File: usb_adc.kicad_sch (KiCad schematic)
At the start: 17 parts, among them IC1 PCM2903CDBR, U3 74LVC1G08, X1 ECS-120-8-36-CKM-TR3

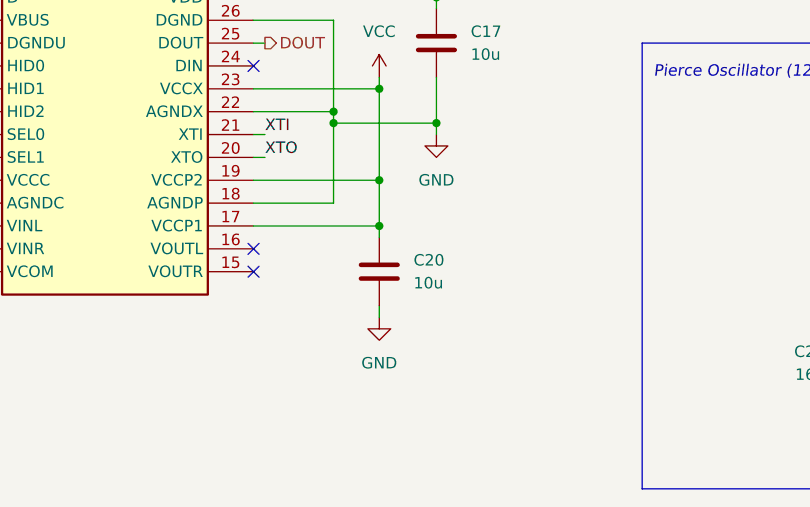
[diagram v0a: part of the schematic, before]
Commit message: Removed S/PIDF and still doing layout
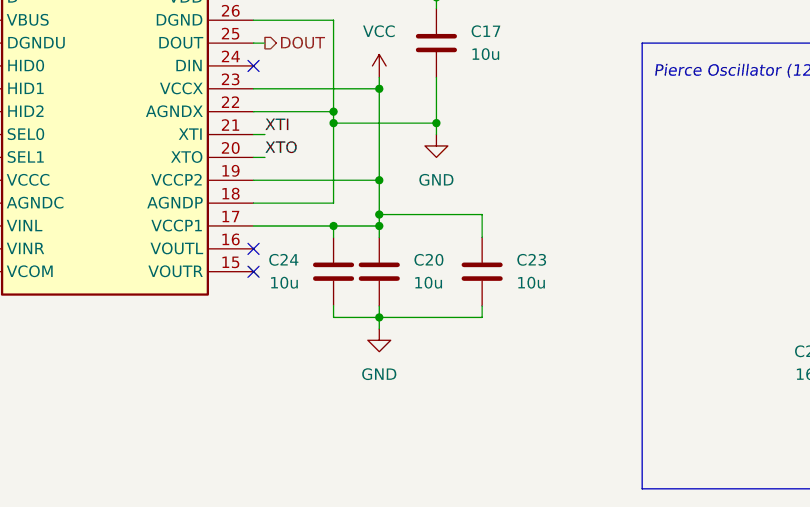
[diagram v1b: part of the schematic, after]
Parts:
- added C23, C24: 10u, Capacitor_SMD:C_0805_2012Metric_Pad1.18x1.45mm_HandSolder, symbol Device:C
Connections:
- net GND: now also C23.2, C24.2
- net VCC: now also C23.1, C24.1

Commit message: More layout, replaced chip crystal with a 2-pin oscillator
All is well with the world
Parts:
- removed X1: ECS-120-8-36-CKM-TR3, binauralmic:ECS120836CKMTR3, symbol Device:Crystal_GND24
- added Y1: ABLS-12.000MHZ-20-D-3-H-T, binauralmic:ABLS, symbol Device:Crystal
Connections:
- net XTI: now also Y1.1
- net XTO: now also Y1.2
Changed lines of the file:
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@@
-	(wire
-		(pts
-			(xy 212.09 107.95) (xy 212.09 109.22)
-		)
-		(stroke
-			(width 0)
-			(type default)
-		)
-	)
-	(wire
-		(pts
-			(xy 208.28 125.73) (xy 208.28 130.81)
-		)
-		(stroke
-			(width 0)
-			(type default)
-		)
-	)
 	(wire
 		(pts
@@
 	(wire
 		(pts
-			(xy 208.28 107.95) (xy 208.28 115.57)
-		)
-		(stroke
-			(width 0)
-			(type default)
-		)
-	)
-	(wire
-		(pts
 			(xy 149.86 85.09) (xy 149.86 86.36)
 		)
@@
 		(pts
 			(xy 187.96 59.69) (xy 190.5 59.69)
-		)
-		(stroke
-			(width 0)
-			(type default)
-		)
-	)
-	(wire
-		(pts
-			(xy 208.28 107.95) (xy 212.09 107.95)
 		)
 		(stroke
@@
 			)
 			(justify right)
+		)
+	)
+	(symbol
+		(lib_id "Device:Crystal")
+		(at 208.28 120.65 0)
+		(unit 1)
+		(exclude_from_sim no)
+		(in_bom yes)
+		(on_board yes)
+		(dnp no)
+		(fields_autoplaced yes)
+		(property "Reference" "Y1"
+			(at 208.28 113.03 0)
+			(effects
+				(font
+					(size 1.27 1.27)
+				)
+			)
+		)
+		(property "Value" "ABLS-12.000MHZ-20-D-3-H-T"
+			(at 208.28 115.57 0)
+			(effects
+				(font
+					(size 1.27 1.27)
+				)
+			)
+		)
+		(property "Footprint" "binauralmic:ABLS"
+			(at 208.28 120.65 0)
+			(effects
+				(font
+					(size 1.27 1.27)
+				)
+				(hide yes)
+			)
+		)
+		(property "Datasheet" "~"
+			(at 208.28 120.65 0)
+			(effects
+				(font
+					(size 1.27 1.27)
+				)
+				(hide yes)
+			)
+		)
+		(property "Description" "Two pin crystal"
+			(at 208.28 120.65 0)
+			(effects
+				(font
+					(size 1.27 1.27)
+				)
+				(hide yes)
+			)
+		)
+		(property "Mouser Part Number" "815-LS12000MHZ20D3HT"
+			(at 208.28 120.65 0)
+			(effects
+				(font
+					(size 1.27 1.27)
+				)
+				(hide yes)
+			)
+		)
+		(pin "2"
+		)
+		(pin "1"
+		)
+		(instances
+			(project ""
+				(path "/d9e790b9-8aa4-4e58-8bd7-6ef4bc890627/1f1de066-50ca-4c06-9457-56cc25f04510"
+					(reference "Y1")
+					(unit 1)
+				)
+			)
 		)
 	)
@@
 				(path "/d9e790b9-8aa4-4e58-8bd7-6ef4bc890627/1f1de066-50ca-4c06-9457-56cc25f04510"
 					(reference "R17")
-					(unit 1)
-				)
-			)
-		)
-	)
-	(symbol
-		(lib_id "power:GND")
-		(at 212.09 109.22 0)
-		(unit 1)
-		(exclude_from_sim no)
-		(in_bom yes)
-		(on_board yes)
-		(dnp no)
-		(fields_autoplaced yes)
-		(property "Reference" "#PWR027"
-			(at 212.09 115.57 0)
-			(effects
-				(font
-					(size 1.27 1.27)
-				)
-				(hide yes)
-			)
-		)
-		(property "Value" "GND"
-			(at 212.09 114.3 0)
-			(effects
-				(font
-					(size 1.27 1.27)
-				)
-			)
-		)
-		(property "Footprint" ""
-			(at 212.09 109.22 0)
-			(effects
-				(font
-					(size 1.27 1.27)
-				)
-				(hide yes)
-			)
-		)
-		(property "Datasheet" ""
-			(at 212.09 109.22 0)
-			(effects
-				(font
-					(size 1.27 1.27)
-				)
-				(hide yes)
-			)
-		)
-		(property "Description" "Power symbol creates a global label with name \"GND\" , ground"
-			(at 212.09 109.22 0)
-			(effects
-				(font
-					(size 1.27 1.27)
-				)
-				(hide yes)
-			)
-		)
-		(pin "1"
-		)
-		(instances
-			(project "BinauralMic"
-				(path "/d9e790b9-8aa4-4e58-8bd7-6ef4bc890627/1f1de066-50ca-4c06-9457-56cc25f04510"
-					(reference "#PWR027")
 					(unit 1)
 				)
@@
 					(unit 1)
 				)
-			)
-		)
-	)
-	(symbol
-		(lib_id "Device:Crystal_GND24")
-		(at 208.28 120.65 0)
-		(mirror y)
-		(unit 1)
-		(exclude_from_sim no)
-		(in_bom yes)
-		(on_board yes)
-		(dnp no)
-		(property "Reference" "X1"
-			(at 224.79 116.586 0)
-			(effects
-				(font
-					(size 1.27 1.27)
-				)
-			)
-		)
-		(property "Value" "ECS-120-8-36-CKM-TR3"
-			(at 225.552 118.872 0)
-			(effects
-				(font
-					(size 1.27 1.27)
-				)
-			)
-		)
-		(property "Footprint" "binauralmic:ECS120836CKMTR3"
-			(at 196.85 129.54 0)
-			(effects
-				(font
-					(size 1.27 1.27)
-				)
-				(hide yes)
-			)
-		)
-		(property "Datasheet" "https://www.mouser.com/datasheet/2/122/ECX_2236-2497269.pdf"
-			(at 212.725 117.475 0)
-			(effects
-				(font
-					(size 1.27 1.27)
-				)
-				(hide yes)
-			)
-		)
-		(property "Description" "Four pin crystal, GND on pins 2 and 4"
-			(at 208.28 120.65 0)
-			(effects
-				(font
-					(size 1.27 1.27)
-				)
-				(hide yes)
-			)
-		)
-		(property "Mouser Part Number" "520-120-8-36-CKM-TR3"
-			(at 208.28 120.65 0)
-			(effects
-				(font
-					(size 1.27 1.27)
-				)
-				(hide yes)
-			)
-		)
-		(pin "2"
-		)
-		(pin "4"
-		)
-		(pin "1"
-		)
-		(pin "3"
-		)
-		(instances
-			(project "BinauralMic"
-				(path "/d9e790b9-8aa4-4e58-8bd7-6ef4bc890627/1f1de066-50ca-4c06-9457-56cc25f04510"
-					(reference "X1")
-					(unit 1)
-				)

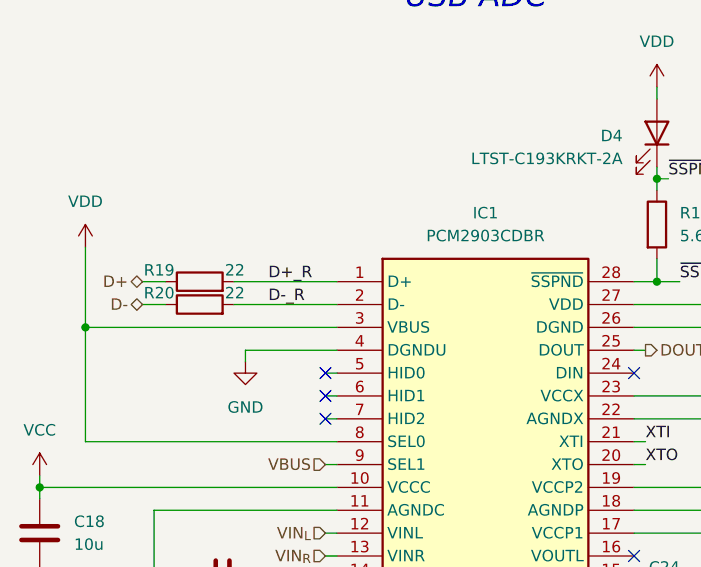
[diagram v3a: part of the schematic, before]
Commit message: Add silkscreen + some bonus test points
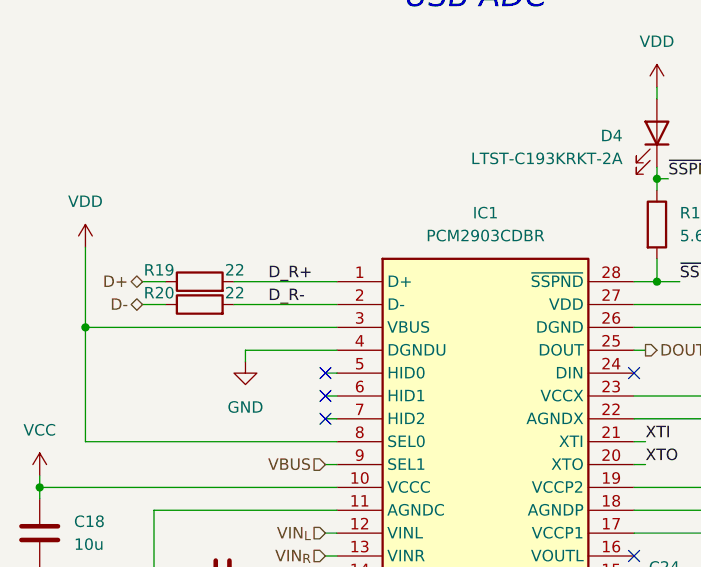
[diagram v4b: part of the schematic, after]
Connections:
- net D+_R renamed D_R+
- net D-_R renamed D_R-
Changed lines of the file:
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@@
 		)
 	)
-	(label "D-_R"
+	(label "D_R-"
 		(at 88.9 85.09 0)
 		(fields_autoplaced yes)
@@
 		)
 	)
-	(label "D+_R"
+	(label "D_R+"
 		(at 88.9 82.55 0)
 		(fields_autoplaced yes)

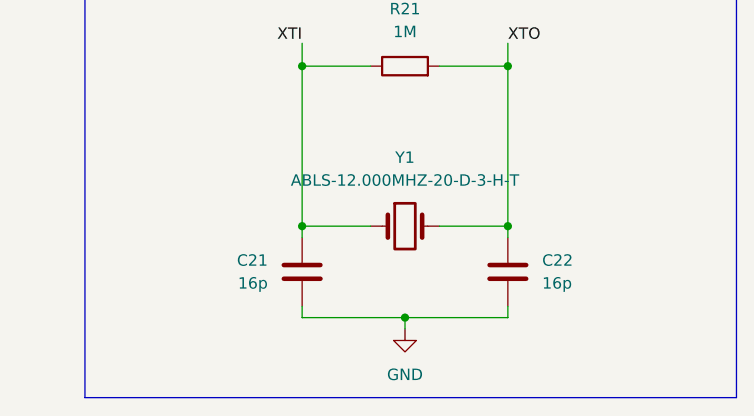
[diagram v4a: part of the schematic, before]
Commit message: Fix pierce osc load caps
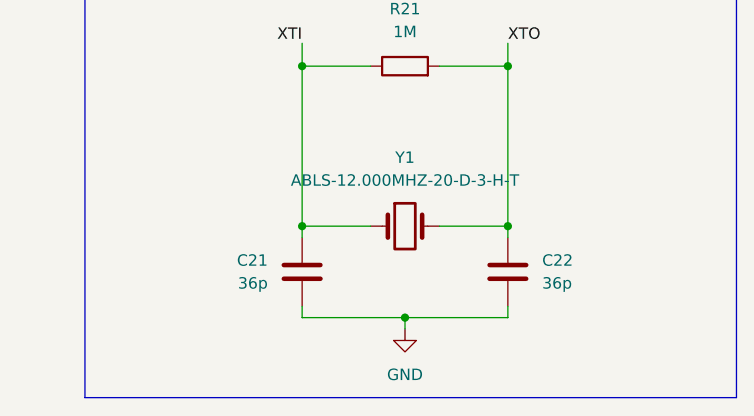
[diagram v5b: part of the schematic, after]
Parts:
- C21, C22: value 16p -> 36p; Mouser Part Number 581-06035A160FAT2A -> 603-CC603FRNPO9BN360
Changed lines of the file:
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@@
 			)
 		)
-		(property "Value" "16p"
+		(property "Value" "36p"
 			(at 223.52 126.9999 0)
 			(effects
@@
 			)
 		)
-		(property "Datasheet" "https://www.mouser.com/datasheet/2/40/C0GNP0_Dielectric-2952720.pdf"
+		(property "Datasheet" "https://www.mouser.com/datasheet/2/447/upy_np0x7r_mv_100_to_630v-3461223.pdf"
 			(at 219.71 125.73 0)
 			(effects
@@
 			)
 		)
-		(property "Mouser Part Number" "581-06035A160FAT2A"
+		(property "Mouser Part Number" "603-CC603FRNPO9BN360"
 			(at 219.71 125.73 0)
 			(effects
@@
 			)
 		)
-		(property "Value" "16p"
+		(property "Value" "36p"
 			(at 193.04 126.9999 0)
 			(effects
@@
 			)
 		)
-		(property "Datasheet" "https://www.mouser.com/datasheet/2/40/C0GNP0_Dielectric-2952720.pdf"
+		(property "Datasheet" "https://www.mouser.com/datasheet/2/447/upy_np0x7r_mv_100_to_630v-3461223.pdf"
 			(at 196.85 125.73 0)
 			(effects
@@
 			)
 		)
-		(property "Mouser Part Number" "581-06035A160FAT2A"
+		(property "Mouser Part Number" "603-CC603FRNPO9BN360"
 			(at 196.85 125.73 0)
 			(effects
